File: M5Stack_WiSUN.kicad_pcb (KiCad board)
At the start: 2 copper layers, 50 x 50 mm, 23 parts, among them J1 MBUS_TOP, J2 MBUS_BOTTOM, J3 AVR_IO, J4 ISP, U1 BP35A1, U2 ATMEGA328P-AU

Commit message: PCB revision B
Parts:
- removed C1, C2, C3, C4: 100n, Capacitor_SMD:C_0402_1005Metric
- removed L1: 10u, Inductor_SMD:L_0603_1608Metric
- removed R1, R4: 0, Resistor_SMD:R_0402_1005Metric
- removed R2, R3, R5, R6: NMT, Resistor_SMD:R_0402_1005Metric
- removed U2: ATMEGA328P-AU, Package_QFP:LQFP-32_7x7mm_P0.8mm
- added J5: PH127-2x3MG, Connector_PinHeader_1.27mm:PinHeader_2x03_P1.27mm_Vertical_SMD, F.Cu at (29.9, 78.9)
- added J6: PH127-2x4MG, Connector_PinHeader_1.27mm:PinHeader_2x04_P1.27mm_Vertical_SMD, F.Cu at (42.0, 78.9)
- added MH7: Fix, MountingHole:MountingHole_2.5mm_Pad, F.Cu at (17.0, 43.0)
- added MH8: Fix, MountingHole:MountingHole_2.5mm_Pad, F.Cu at (53.0, 43.0)
- J3: value AVR_IO -> PH127-2x4MG; footprint Connector_PinHeader_2.54mm:PinHeader_1x09_P2.54mm_Vertical -> Connector_PinHeader_1.27mm:PinHeader_2x04_P1.27mm_Vertical_SMD
- J4: value ISP -> PH127-2x3MG; footprint Connector_PinHeader_2.54mm:PinHeader_2x03_P2.54mm_Vertical -> Connector_PinHeader_1.27mm:PinHeader_2x03_P1.27mm_Vertical_SMD
- MH5, MH6: footprint MountingHole:MountingHole_2.5mm -> MountingHole:MountingHole_2.5mm_Pad
- moved J3 32.4 mm to (35.6, 78.9), turned to 270 degrees
- moved J4 3.79 mm to (24.8, 78.9), turned to 270 degrees
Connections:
- J3 pad 1: /AVR_ADC3 -> /BP35_RESET
- J3 pad 2: /AVR_ADC2 -> /GPIO_G5
- J3 pad 3: /AVR_ADC1 -> /BP35_RESET
- J3 pad 4: /AVR_ADC0 -> /IIS_WS
- J3 pad 5: /AVR_PB1 -> /BP35_WKUP
- J3 pad 6: /AVR_PD4 -> /GPIO_G2
- J3 pad 7: /AVR_PD5 -> /BP35_WKUP
- J3 pad 8: +3V3 -> /IIS_SK
- J4 pad 1: /AVR_MISO -> /BP35_TXD
- J4 pad 2: +3V3 -> /RXD2
- J4 pad 3: /AVR_SCK -> /BP35_TXD
- J4 pad 4: /AVR_MOSI -> /GPIO_G2
- J4 pad 5: /AVR_RESET -> /BP35_TXD
- J4 pad 6: GND -> /IIS_SK
- U1 pad 16: (no net) -> Net-(U1-Pad16)
- U1 pad 17: (no net) -> Net-(U1-Pad17)
- U1 pad 18: (no net) -> Net-(U1-Pad18)
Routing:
- net /AVR_ADC2: track 58.3 -> 0.00 mm
- net /IIS_SK: track 14.6 -> 68.9 mm, vias 2 -> 4
- net /AVR_ADC1: track 51.9 -> 0.00 mm, vias 1 -> 0
- net /RXD2: track 5.07 -> 51.9 mm, vias 1 -> 2
- net /AVR_ADC0: track 44.8 -> 0.00 mm, vias 1 -> 0
- net /AVR_ADC3: track 43.5 -> 0.00 mm, vias 1 -> 0
- net +3V3: track 74.9 -> 32.1 mm, vias 7 -> 2
- net /GPIO_G2: track 16.3 -> 56.7 mm, vias 2 -> 3
- net /IIS_WS: track 14.5 -> 53.0 mm, vias 1 -> 4
- net /TXD2: track 5.13 -> 42.6 mm, vias 1 -> 2
- net /IIS_OUT: track 2.55 -> 37.4 mm, vias 1 -> 2
- net /AVR_PB1: track 32.3 -> 0.00 mm, vias 1 -> 0
- net /AVR_PD4: track 30.3 -> 0.00 mm, vias 1 -> 0
- net /SDA: track 35.1 -> 5.05 mm
- net /GPIO_G5: track 15.8 -> 44.2 mm, vias 1 -> 3
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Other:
- outline, holes or cut-outs redrawn
- board text added: "CTS"
- board text added: "G0"
- board text added: "G12"
- board text added: "G13"
- board text added: "G15"
- board text added: "G16"
- board text added: "G17"
- board text added: "G2"
- board text added: "G5"
- board text added: "M5_RXD"
- board text added: "M5_TXD"
- board text added: "RST"
- board text added: "RTS"
- board text added: "WK"
- board text added: "Wi-SUN Stack for M5Stack Rev.B"
- board text removed: "Wi-SUN Stack for M5Stack Rev.A"

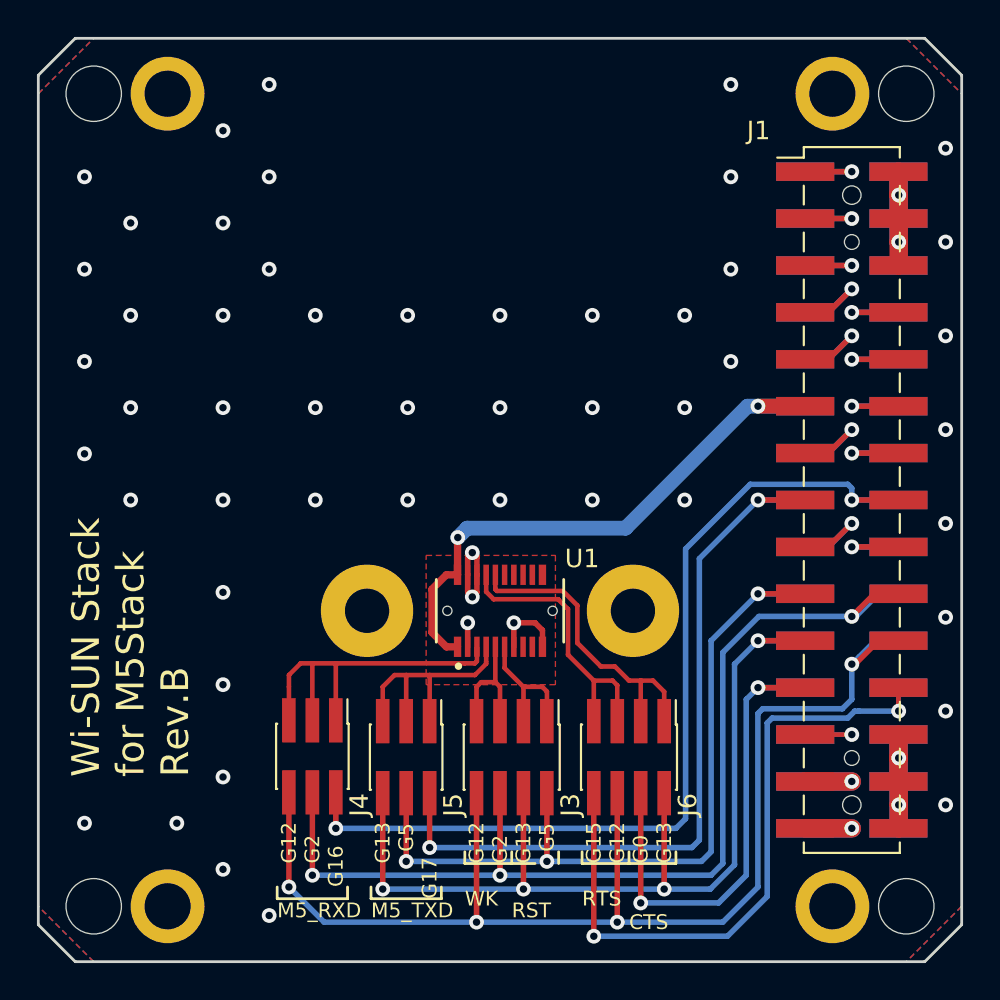
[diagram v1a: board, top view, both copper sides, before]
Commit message: Move BP35A1 to bottom side. Use I2C IO expander to control BP35A1 reset and wake pins.
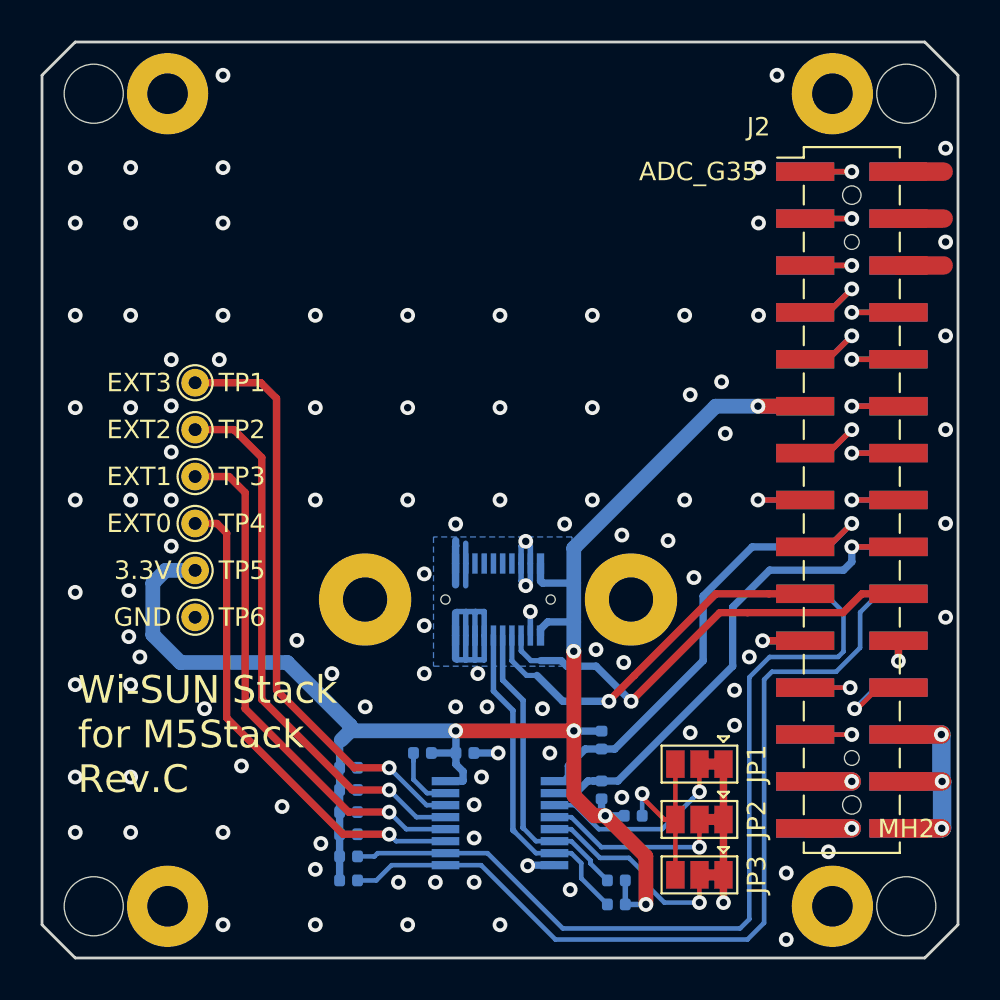
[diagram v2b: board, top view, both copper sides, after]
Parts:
- removed J3, J6: PH127-2x4MG, Connector_PinHeader_1.27mm:PinHeader_2x04_P1.27mm_Vertical_SMD
- removed J4, J5: PH127-2x3MG, Connector_PinHeader_1.27mm:PinHeader_2x03_P1.27mm_Vertical_SMD
- added C1: 100n, Capacitor_SMD:C_0402_1005Metric, B.Cu at (33.1, 78.7)
- added JP1: Jumper_3_Bridged12, Jumper:SolderJumper-3_P1.3mm_Bridged12_Pad1.0x1.5mm, F.Cu at (45.8, 79.3)
- added JP2: Jumper_3_Bridged12, Jumper:SolderJumper-3_P1.3mm_Bridged12_Pad1.0x1.5mm, F.Cu at (45.8, 82.3)
- added JP3: Jumper_3_Bridged12, Jumper:SolderJumper-3_P1.3mm_Bridged12_Pad1.0x1.5mm, F.Cu at (45.8, 85.3)
- added R1: 2k, Resistor_SMD:R_0402_1005Metric, B.Cu at (40.5, 78.0)
- added R10: 100k, Resistor_SMD:R_0402_1005Metric, B.Cu at (26.8, 85.6)
- added R11: 100k, Resistor_SMD:R_0402_1005Metric, B.Cu at (41.3, 86.9)
- added R12: 100k, Resistor_SMD:R_0402_1005Metric, B.Cu at (41.3, 85.6)
- added R2: 2k, Resistor_SMD:R_0402_1005Metric, B.Cu at (42.2, 82.1)
- added R3: 2k, Resistor_SMD:R_0402_1005Metric, B.Cu at (30.8, 78.7)
- added R4: 2k, Resistor_SMD:R_0402_1005Metric, B.Cu at (40.5, 80.7)
- added R5: 100k, Resistor_SMD:R_0402_1005Metric, B.Cu at (26.8, 79.5)
- added R6: 100k, Resistor_SMD:R_0402_1005Metric, B.Cu at (26.8, 80.7)
- added R7: 100k, Resistor_SMD:R_0402_1005Metric, B.Cu at (26.8, 81.9)
- added R8: 100k, Resistor_SMD:R_0402_1005Metric, B.Cu at (26.8, 83.1)
- added R9: 100k, Resistor_SMD:R_0402_1005Metric, B.Cu at (26.8, 84.3)
- added TP1: TestPoint, TestPoint:TestPoint_THTPad_D1.5mm_Drill0.7mm, F.Cu at (18.5, 58.6)
- added TP2: TestPoint, TestPoint:TestPoint_THTPad_D1.5mm_Drill0.7mm, F.Cu at (18.5, 61.2)
- added TP3: TestPoint, TestPoint:TestPoint_THTPad_D1.5mm_Drill0.7mm, F.Cu at (18.5, 63.7)
- added TP4: TestPoint, TestPoint:TestPoint_THTPad_D1.5mm_Drill0.7mm, F.Cu at (18.5, 66.3)
- added TP5: TestPoint, TestPoint:TestPoint_THTPad_D1.5mm_Drill0.7mm, F.Cu at (18.5, 68.8)
- added TP6: TestPoint, TestPoint:TestPoint_THTPad_D1.5mm_Drill0.7mm, F.Cu at (18.5, 71.3)
- added U2: PCA9557, Package_SO:TSSOP-16_4.4x5mm_P0.65mm, B.Cu at (35.0, 82.5)
- J1: value MBUS_TOP -> MBUS_BOTTOM; footprint local:MBUS_Header -> local:MBUS_Socket; moved to B.Cu
- J2: value MBUS_BOTTOM -> MBUS_TOP; footprint local:MBUS_Socket -> local:MBUS_Header; moved to F.Cu
- MH1, MH2, MH3, MH4: footprint MountingHole:MountingHole_3mm -> MountingHole:MountingHole_3.2mm_M3
- MH5, MH6, MH7, MH8: footprint MountingHole:MountingHole_2.5mm_Pad -> MountingHole:MountingHole_2.2mm_M2_Pad
- U1: moved to B.Cu
- moved U1 0.62 mm to (34.9, 70.4), turned to 180 degrees
- turned J1 to 180 degrees
- turned J2 to 0 degrees
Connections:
- J1 pad 1: /ADC_G35 -> GND
- J1 pad 10: /MISO -> /DAC
- J1 pad 11: +3V3 -> /SCK
- J1 pad 12: /SCK -> +3V3
- J1 pad 13: /TXD0 -> /RXD0
- J1 pad 14: /RXD0 -> /TXD0
- J1 pad 15: /TXD2 -> /RXD2
- J1 pad 16: /RXD2 -> /TXD2
- J1 pad 17: /SCL -> /SDA
- J1 pad 18: /SDA -> /SCL
- J1 pad 19: /GPIO_G5 -> /GPIO_G2_R
- J1 pad 2: GND -> /ADC_G35
- J1 pad 20: /GPIO_G2 -> /GPIO_G5_R
- J1 pad 21: /IIS_WS -> /IIS_SK
- J1 pad 22: /IIS_SK -> /IIS_WS
- J1 pad 23: /IIS_MK -> /IIS_OUT
- J1 pad 24: /IIS_OUT -> /IIS_MK
- J1 pad 25: /IIS_IN -> /HPWR
- J1 pad 26: /HPWR -> /IIS_IN
- J1 pad 27: +5V -> /HPWR
- J1 pad 28: /HPWR -> +5V
- J1 pad 29: /BATTERY -> /HPWR
- J1 pad 3: /ADC_G36 -> GND
- J1 pad 30: /HPWR -> /BATTERY
- J1 pad 4: GND -> /ADC_G36
- J1 pad 5: /RST -> GND
- J1 pad 6: GND -> /RST
- J1 pad 7: /DAC_SPK -> /MOSI
- J1 pad 8: /MOSI -> /DAC_SPK
- J1 pad 9: /DAC -> /MISO
- J2 pad 1: GND -> /ADC_G35
- J2 pad 10: /DAC -> /MISO
- J2 pad 11: /SCK -> +3V3
- J2 pad 12: +3V3 -> /SCK
- J2 pad 13: /RXD0 -> /TXD0
- J2 pad 14: /TXD0 -> /RXD0
- J2 pad 15: /RXD2 -> /TXD2
- J2 pad 16: /TXD2 -> /RXD2
- J2 pad 17: /SDA -> /SCL
- J2 pad 18: /SCL -> /SDA
- J2 pad 19: /GPIO_G2 -> /GPIO_G5
- J2 pad 2: /ADC_G35 -> GND
- J2 pad 20: /GPIO_G5 -> /GPIO_G2
- J2 pad 21: /IIS_SK -> /IIS_WS
- J2 pad 22: /IIS_WS -> /IIS_SK
- J2 pad 23: /IIS_OUT -> /IIS_MK
- J2 pad 24: /IIS_MK -> /IIS_OUT
- J2 pad 25: /HPWR -> /IIS_IN
- J2 pad 26: /IIS_IN -> /HPWR
- J2 pad 27: /HPWR -> +5V
- J2 pad 28: +5V -> /HPWR
- J2 pad 29: /HPWR -> /BATTERY
- J2 pad 3: GND -> /ADC_G36
- J2 pad 30: /BATTERY -> /HPWR
- J2 pad 4: /ADC_G36 -> GND
- J2 pad 5: GND -> /RST
- J2 pad 6: /RST -> GND
- J2 pad 7: /MOSI -> /DAC_SPK
- J2 pad 8: /DAC_SPK -> /MOSI
- J2 pad 9: /MISO -> /DAC
- U1 pad 14: /BP35_CTS -> (no net)
- U1 pad 15: /BP35_RTS -> (no net)
- U1 pad 16: Net-(U1-Pad16) -> (no net)
- U1 pad 17: Net-(U1-Pad17) -> (no net)
- U1 pad 18: Net-(U1-Pad18) -> (no net)
- U1 pad 3: /BP35_TXD -> /GPIO_G2
- U1 pad 4: /BP35_RXD -> /GPIO_G5
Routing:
- net /IIS_SK: track 68.9 -> 4.54 mm, vias 4 -> 1
- net +3V3: track 32.1 -> 94.6 mm, vias 2 -> 6
- net /IIS_WS: track 53.0 -> 4.61 mm, vias 4 -> 1
- net /GPIO_G2_R: track 0.00 -> 47.9 mm
- net /RXD2: track 51.9 -> 5.05 mm, vias 2 -> 1
- net /GPIO_G5_R: track 0.00 -> 46.6 mm
- net /TXD2: track 42.6 -> 5.11 mm, vias 2 -> 1
- net /EXT3: track 0.00 -> 34.0 mm, vias 0 -> 1
- net /IIS_OUT: track 37.4 -> 5.72 mm, vias 2 -> 1
- net /EXT2: track 0.00 -> 31.6 mm, vias 0 -> 1
- net /GPIO_G2: track 56.7 -> 26.3 mm, vias 3 -> 1
- net GND: track 19.4 -> 49.7 mm, vias 56 -> 106
- net /EXT1: track 0.00 -> 30.0 mm, vias 0 -> 1
- net /EXT0: track 0.00 -> 28.3 mm, vias 0 -> 1
- net /SDA: track 5.05 -> 29.0 mm
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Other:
- board size 50 x 50 mm -> 49.6 x 49.6 mm
- board text added: "3.3V"
- board text added: "ADC_G35"
- board text added: "EXT0"
- board text added: "EXT1"
- board text added: "EXT2"
- board text added: "EXT3"
- board text added: "GND"
- board text added: "Wi-SUN Stack for M5Stack Rev.C"
- board text removed: "CTS"
- board text removed: "G0"
- board text removed: "G12"
- board text removed: "G13"
- board text removed: "G15"
- board text removed: "G16"
- board text removed: "G17"
- board text removed: "G2"
- board text removed: "G5"
- board text removed: "M5_RXD"
- board text removed: "M5_TXD"
- board text removed: "RST"
- board text removed: "RTS"
- board text removed: "WK"
- board text removed: "Wi-SUN Stack for M5Stack Rev.B"
